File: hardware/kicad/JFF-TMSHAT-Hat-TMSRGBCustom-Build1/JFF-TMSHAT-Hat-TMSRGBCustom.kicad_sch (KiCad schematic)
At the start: 44 parts, among them J13 AV EXT, J5 RGB, U1 CD74HC4053PWR, U2 LM1881MX/NOPB, U3 MAX4395EUD, U4 TS5A4597DCKR, U5 SN74LVC2G17DCKR, U6 LMH1251MT/NOPB, U7 THS7374IPWR

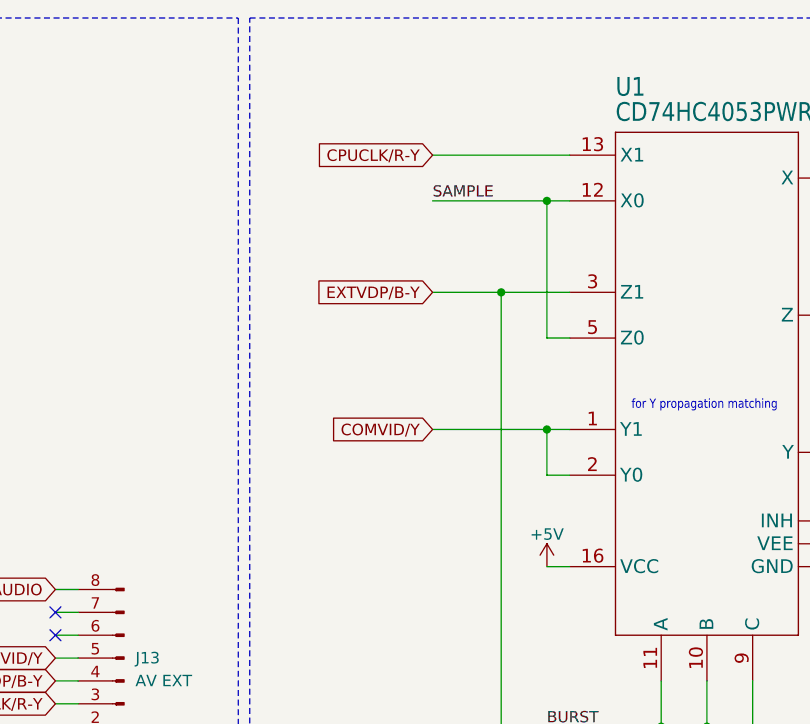
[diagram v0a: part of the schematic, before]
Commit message: tmshats: add missing Y,R-Y,B-Y resistors
Signed-off-by: Albert Herranz <albert_herranz@yahoo.es>
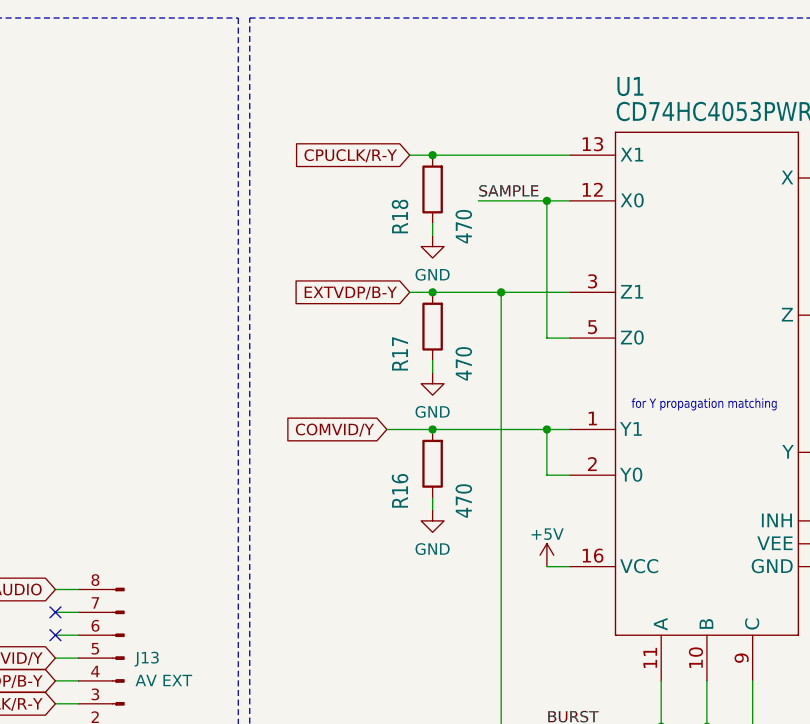
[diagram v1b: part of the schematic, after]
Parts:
- added R16, R17, R18: 470, Resistor_SMD:R_0805_2012Metric_Pad1.20x1.40mm_HandSolder, symbol Device:R
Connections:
- net COMVID/Y: now also R16.2
- net CPUCLK/R-Y: now also R18.2
- net EXTVDP/B-Y: now also R17.2
- net GND: now also R16.1, R17.1, R18.1
